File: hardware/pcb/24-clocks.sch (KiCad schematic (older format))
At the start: 2 parts

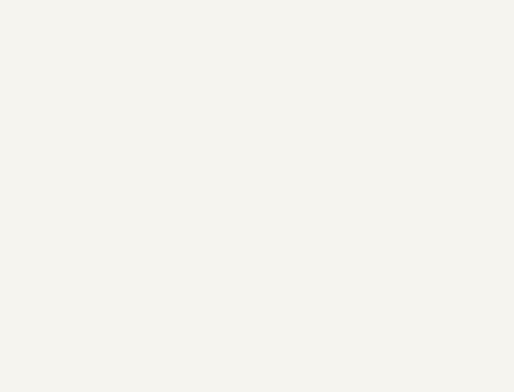
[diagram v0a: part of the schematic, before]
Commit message: Created PCB outline and first placement
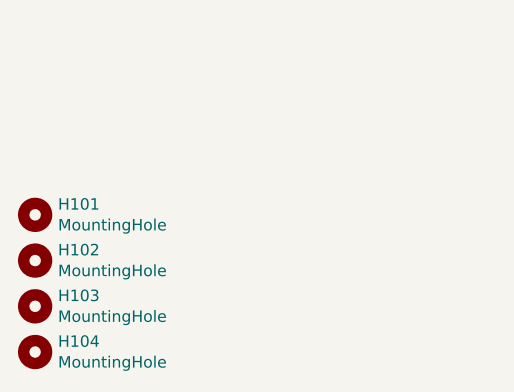
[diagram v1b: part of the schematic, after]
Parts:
- added H101, H102, H103, H104: MountingHole, MountingHole:MountingHole_3.2mm_M3, symbol Mechanical:MountingHole
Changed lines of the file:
@@
 Wire Wire Line
 	3700 5350 4750 5350
+$Comp
+L Mechanical:MountingHole H101
+U 1 1 5FEC3F65
+P 650 7000
+F 0 "H101" H 750 7046 50  0000 L CNN
+F 1 "MountingHole" H 750 6955 50  0000 L CNN
+F 2 "MountingHole:MountingHole_3.2mm_M3" H 650 7000 50  0001 C CNN
+F 3 "~" H 650 7000 50  0001 C CNN
+	1    650  7000
+	1    0    0    -1
+$EndComp
+$Comp
+L Mechanical:MountingHole H102
+U 1 1 5FEC5189
+P 650 7200
+F 0 "H102" H 750 7246 50  0000 L CNN
+F 1 "MountingHole" H 750 7155 50  0000 L CNN
+F 2 "MountingHole:MountingHole_3.2mm_M3" H 650 7200 50  0001 C CNN
+F 3 "~" H 650 7200 50  0001 C CNN
+	1    650  7200
+	1    0    0    -1
+$EndComp
+$Comp
+L Mechanical:MountingHole H103
+U 1 1 5FEC5459
+P 650 7400
+F 0 "H103" H 750 7446 50  0000 L CNN
+F 1 "MountingHole" H 750 7355 50  0000 L CNN
+F 2 "MountingHole:MountingHole_3.2mm_M3" H 650 7400 50  0001 C CNN
+F 3 "~" H 650 7400 50  0001 C CNN
+	1    650  7400
+	1    0    0    -1
+$EndComp
+$Comp
+L Mechanical:MountingHole H104
+U 1 1 5FEC567F
+P 650 7600
+F 0 "H104" H 750 7646 50  0000 L CNN
+F 1 "MountingHole" H 750 7555 50  0000 L CNN
+F 2 "MountingHole:MountingHole_3.2mm_M3" H 650 7600 50  0001 C CNN
+F 3 "~" H 650 7600 50  0001 C CNN
+	1    650  7600
+	1    0    0    -1
+$EndComp
 $EndSCHEMATC

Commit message: Changed supply to 7V
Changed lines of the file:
@@
 EESchema Schematic File Version 4
-LIBS:24-clocks-cache
-EELAYER 29 0
+EELAYER 30 0
 EELAYER END
 $Descr A4 11693 8268
@@
 F0 "Power Supply" 50
 F1 "24-c-supply.sch" 50
-F2 "+9V" I L 1750 1950 50
+F2 "+7V" I L 1750 1950 50
 F3 "+5V" O R 2900 1950 50
 F4 "+3V3" O R 2900 2300 50

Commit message: First placement
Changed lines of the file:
@@
 $EndDescr
-$Comp
-L power:+9V #PWR0101
-U 1 1 5FC806BB
-P 1400 1850
-F 0 "#PWR0101" H 1400 1700 50  0001 C CNN
-F 1 "+9V" H 1415 2023 50  0000 C CNN
-F 2 "" H 1400 1850 50  0001 C CNN
-F 3 "" H 1400 1850 50  0001 C CNN
-	1    1400 1850
-	1    0    0    -1
-$EndComp
 $Comp
 L power:+5V #PWR0102
@@
 	1    0    0    -1
 $EndComp
+$Comp
+L power:+7.5V #PWR0101
+U 1 1 60073D60
+P 1400 1850
+F 0 "#PWR0101" H 1400 1700 50  0001 C CNN
+F 1 "+7.5V" H 1415 2023 50  0000 C CNN
+F 2 "" H 1400 1850 50  0001 C CNN
+F 3 "" H 1400 1850 50  0001 C CNN
+	1    1400 1850
+	1    0    0    -1
+$EndComp

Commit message: Added routing
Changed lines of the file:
@@
 I2C-SDA
 $Sheet
-S 5400 1700 1750 3900
+S 5400 1700 1750 4000
 U 5FDEAABE
 F0 "uC" 50
@@
 F14 "I2C-SCL" O L 5400 5200 50
 F15 "I2C-SDA" B L 5400 5350 50
+F16 "RTC-CLK" I L 5400 5500 50
 $EndSheet
 $Sheet
@@
 $EndSheet
 $Sheet
-S 2600 4950 1100 650
+S 2600 4950 1100 750
 U 5FDBDABC
 F0 "RTC and Memory" 50
@@
 F2 "I2C-SDA" B R 3700 5350 50
 F3 "I2C-SCL" I R 3700 5200 50
+F4 "RTC-CLK" O R 3700 5500 50
 $EndSheet
 Wire Wire Line
@@
 	1    0    0    -1
 $EndComp
+Wire Wire Line
+	3700 5500 5400 5500
 $EndSCHEMATC
